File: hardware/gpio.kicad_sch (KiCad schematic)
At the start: 19 parts, among them J3 HDMI_C_1.3, U5 PCA9306DC1

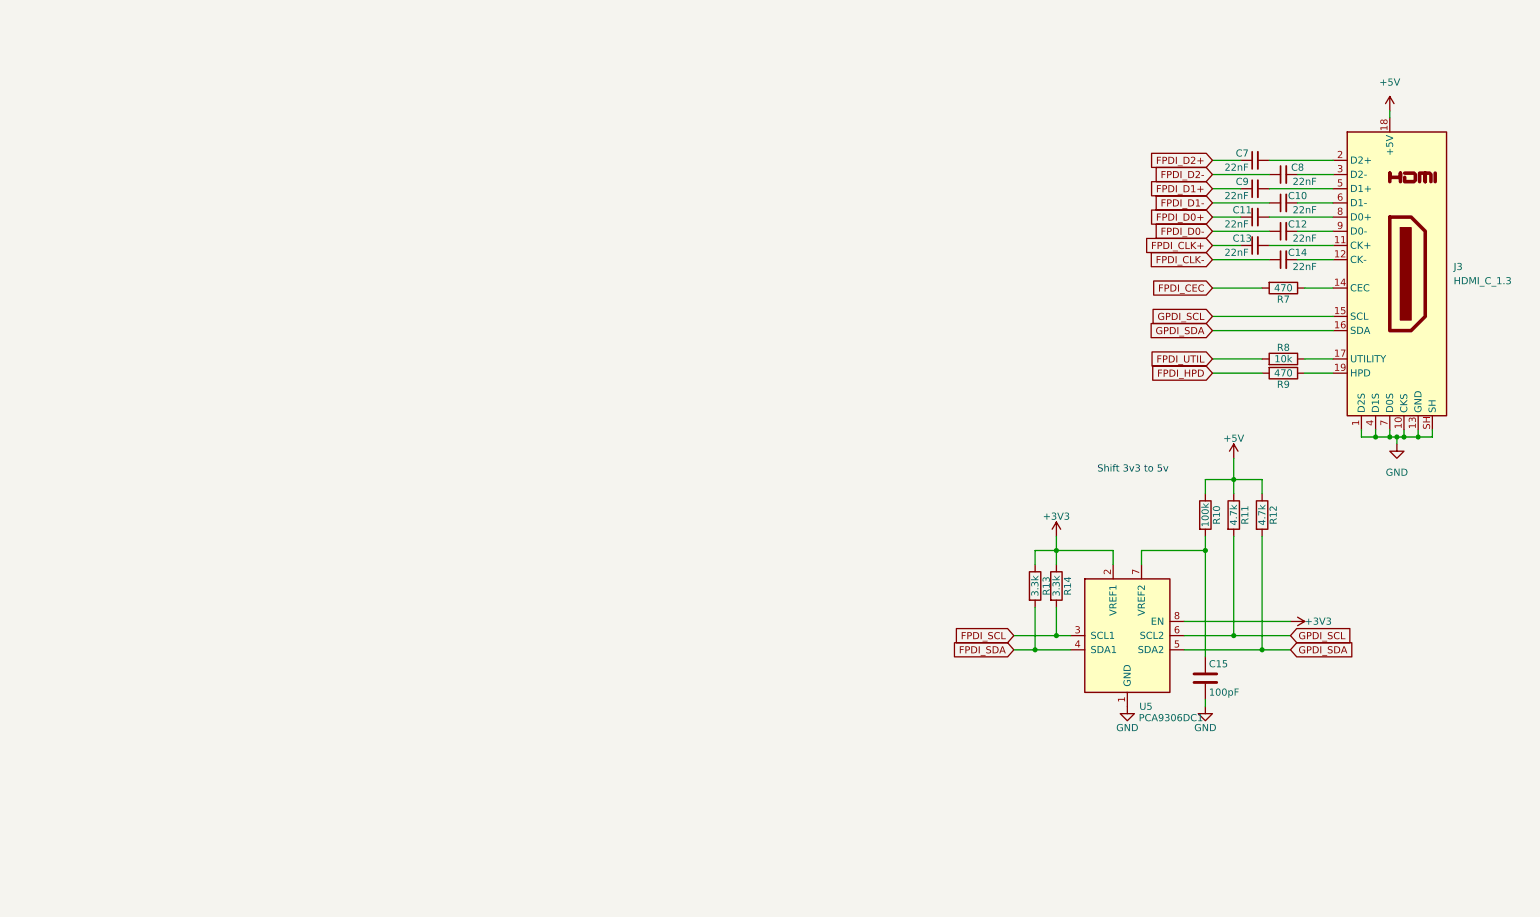
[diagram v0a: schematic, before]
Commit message: Routed most of sdram
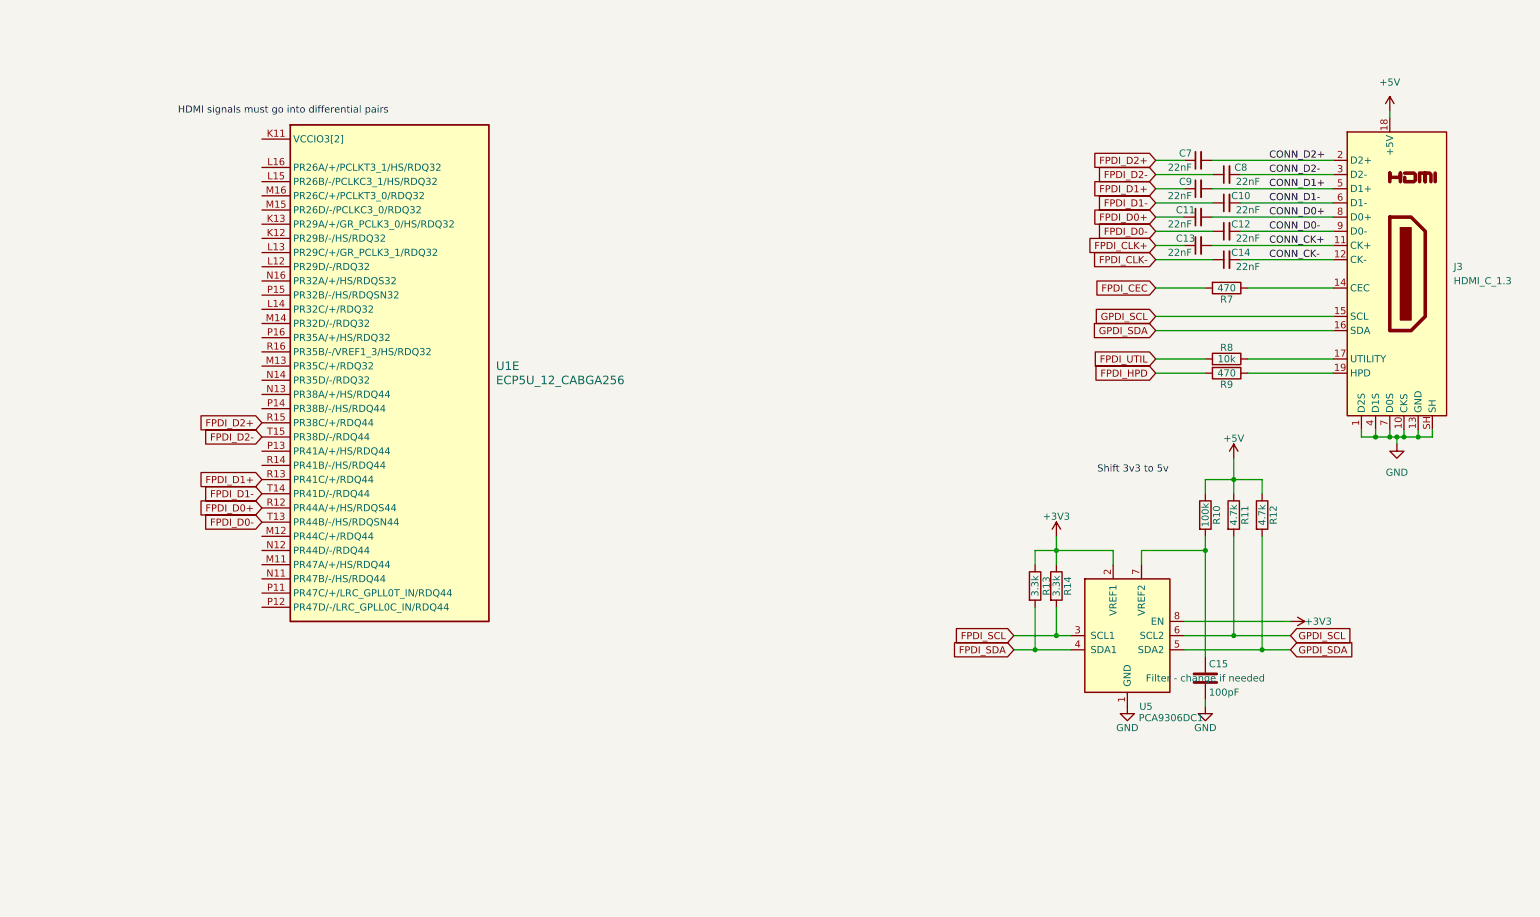
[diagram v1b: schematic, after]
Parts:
- added U1: ECP5U_12_CABGA256, Package_BGA:BGA-256_14.0x14.0mm_Layout16x16_P0.8mm_Ball0.45mm_Pad0.32mm_NSMD, symbol josh:ECP5U_12_CABGA256
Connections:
- net FPDI_D0+: now also U1.R12 (PR44A/+/HS/RDQS44)
- net FPDI_D0-: now also U1.T13 (PR44B/-/HS/RDQSN44)
- net FPDI_D1+: now also U1.R13 (PR41C/+/RDQ44)
- net FPDI_D1-: now also U1.T14 (PR41D/-/RDQ44)
- net FPDI_D2+: now also U1.R15 (PR38C/+/RDQ44)
- net FPDI_D2-: now also U1.T15 (PR38D/-/RDQ44)
- net CONN_D0+: now reaches C11.2, J3.8 (D0+)
- net CONN_D1+: now reaches C9.2, J3.5 (D1+)
- net CONN_D0-: now reaches C12.2, J3.9 (D0-)
- net CONN_CK-: now reaches C14.2, J3.12 (CK-)
- net CONN_D1-: now reaches C10.2, J3.6 (D1-)
- net CONN_D2+: now reaches C7.2, J3.2 (D2+)
- net CONN_CK+: now reaches C13.2, J3.11 (CK+)
- net CONN_D2-: now reaches C8.2, J3.3 (D2-)
- new net: U1.K11 (VCCIO3[2]), U1.L11 (VCCIO3[2])
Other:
- note added: "HDMI signals must go into differential pairs"
- moved on the sheet: C10, C11, C12, C13, C14, C7, C8, C9, R7, R8, R9

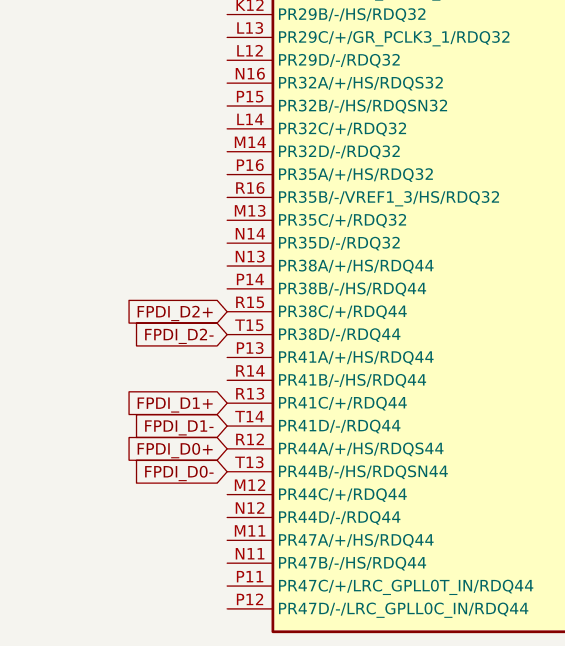
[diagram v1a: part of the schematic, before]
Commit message: Routed power
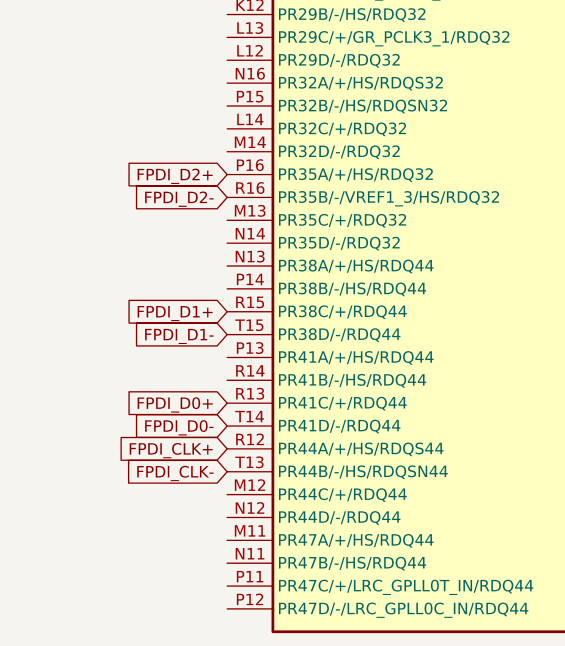
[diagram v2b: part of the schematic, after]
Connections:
- net FPDI_CLK+: now also U1.R12 (PR44A/+/HS/RDQS44)
- net FPDI_CLK-: now also U1.T13 (PR44B/-/HS/RDQSN44)
- net FPDI_D0+: now also U1.R13 (PR41C/+/RDQ44); no longer U1.R12 (PR44A/+/HS/RDQS44)
- net FPDI_D0-: now also U1.T14 (PR41D/-/RDQ44); no longer U1.T13 (PR44B/-/HS/RDQSN44)
- net FPDI_D1+: now also U1.R15 (PR38C/+/RDQ44); no longer U1.R13 (PR41C/+/RDQ44)
- net FPDI_D1-: now also U1.T15 (PR38D/-/RDQ44); no longer U1.T14 (PR41D/-/RDQ44)
- net FPDI_D2+: now also U1.P16 (PR35A/+/HS/RDQ32); no longer U1.R15 (PR38C/+/RDQ44)
- net FPDI_D2-: now also U1.R16 (PR35B/-/VREF1_3/HS/RDQ32); no longer U1.T15 (PR38D/-/RDQ44)

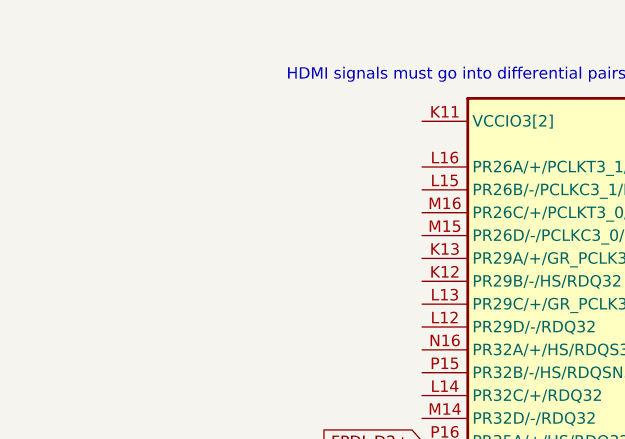
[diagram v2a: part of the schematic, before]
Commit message: Added the decoupling capacitors
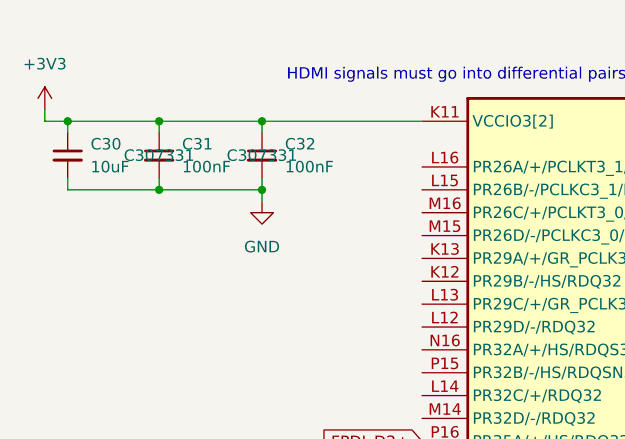
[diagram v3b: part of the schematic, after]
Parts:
- added C30: 10uF, Capacitor_SMD:C_0603_1608Metric, symbol Device:C_Small
- added C31, C32: 100nF, Capacitor_SMD:C_0402_1005Metric, symbol Device:C_Small
- C10, C11, C12, C13, C14, C7, C8, C9: JLCPCB Part # (none) -> C1532
- C15: JLCPCB Part # (none) -> C1546
- J3: footprint cyao:XKB Connection A71-05H4-111N1 -> icepi-lib:XKB Connection A71-05H4-111N1
- R10: JLCPCB Part # (none) -> C25741
- R11, R12: JLCPCB Part # (none) -> C25900
- R13, R14: JLCPCB Part # (none) -> C25890
- R7, R9: JLCPCB Part # (none) -> C25117
- R8: JLCPCB Part # (none) -> C25744
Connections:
- net +3V3: now also U1.K11 (VCCIO3[2]), U1.L11 (VCCIO3[2]), C30.1, C31.1, C32.1
- net GND: now also C30.2, C31.2, C32.2

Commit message: V1.0 Final Revision and Readme documentation
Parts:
- removed U1: ECP5U_12_CABGA256, Package_BGA:BGA-256_14.0x14.0mm_Layout16x16_P0.8mm_Ball0.45mm_Pad0.32mm_NSMD, symbol josh:ECP5U_12_CABGA256
- added U3: ECP5U_12_CABGA256, Package_BGA:BGA-256_14.0x14.0mm_Layout16x16_P0.8mm_Ball0.45mm_Pad0.32mm_NSMD, symbol josh:ECP5U_12_CABGA256
- renumbered C7 to C21, C8 to C22, C9 to C23, C10 to C24, C11 to C25, C12 to C26, C13 to C27, C14 to C28, C15 to C29, C30 to C44, C31 to C45, C32 to C46, J3 to J2, R10 to R11, R11 to R12, R12 to R13, R13 to R14, R14 to R15, R7 to R16, R8 to R17, R9 to R18
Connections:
- net +3V3: now also U3.K11 (VCCIO3[2]), U3.L11 (VCCIO3[2])
- net FPDI_CLK+: now also U3.R12 (PR44A/+/HS/RDQS44)
- net FPDI_CLK-: now also U3.T13 (PR44B/-/HS/RDQSN44)
- net FPDI_D0+: now also U3.R13 (PR41C/+/RDQ44)
- net FPDI_D0-: now also U3.T14 (PR41D/-/RDQ44)
- net FPDI_D1+: now also U3.R15 (PR38C/+/RDQ44)
- net FPDI_D1-: now also U3.T15 (PR38D/-/RDQ44)
- net FPDI_D2+: now also U3.P16 (PR35A/+/HS/RDQ32)
- net FPDI_D2-: now also U3.R16 (PR35B/-/VREF1_3/HS/RDQ32)
- net FPDI_HPD: now also U3.L14 (PR32C/+/RDQ32)
- new net SD_CLK: U3.N16 (PR32A/+/HS/RDQS32)
- new net SD_CMD: U3.P15 (PR32B/-/HS/RDQSN32)
- new net SD_DAT0: U3.P14 (PR38B/-/HS/RDQ44)
- new net SD_DAT1: U3.R14 (PR41B/-/HS/RDQ44)
- new net SD_DAT2: U3.M15 (PR26D/-/PCLKC3_0/RDQ32)
- new net SD_DAT3: U3.M14 (PR32D/-/RDQ32)
- new net SD_DET: U3.M16 (PR26C/+/PCLKT3_0/RDQ32)
- new net ~{USB_DTR}: U3.L15 (PR26B/-/PCLKC3_1/HS/RDQ32)
- new net ~{USB_RTS}: U3.L16 (PR26A/+/PCLKT3_1/HS/RDQ32)
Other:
- moved on the sheet: C21, C22, C23, C24, C25, C26, C27, C28, C29, C44, C45, C46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

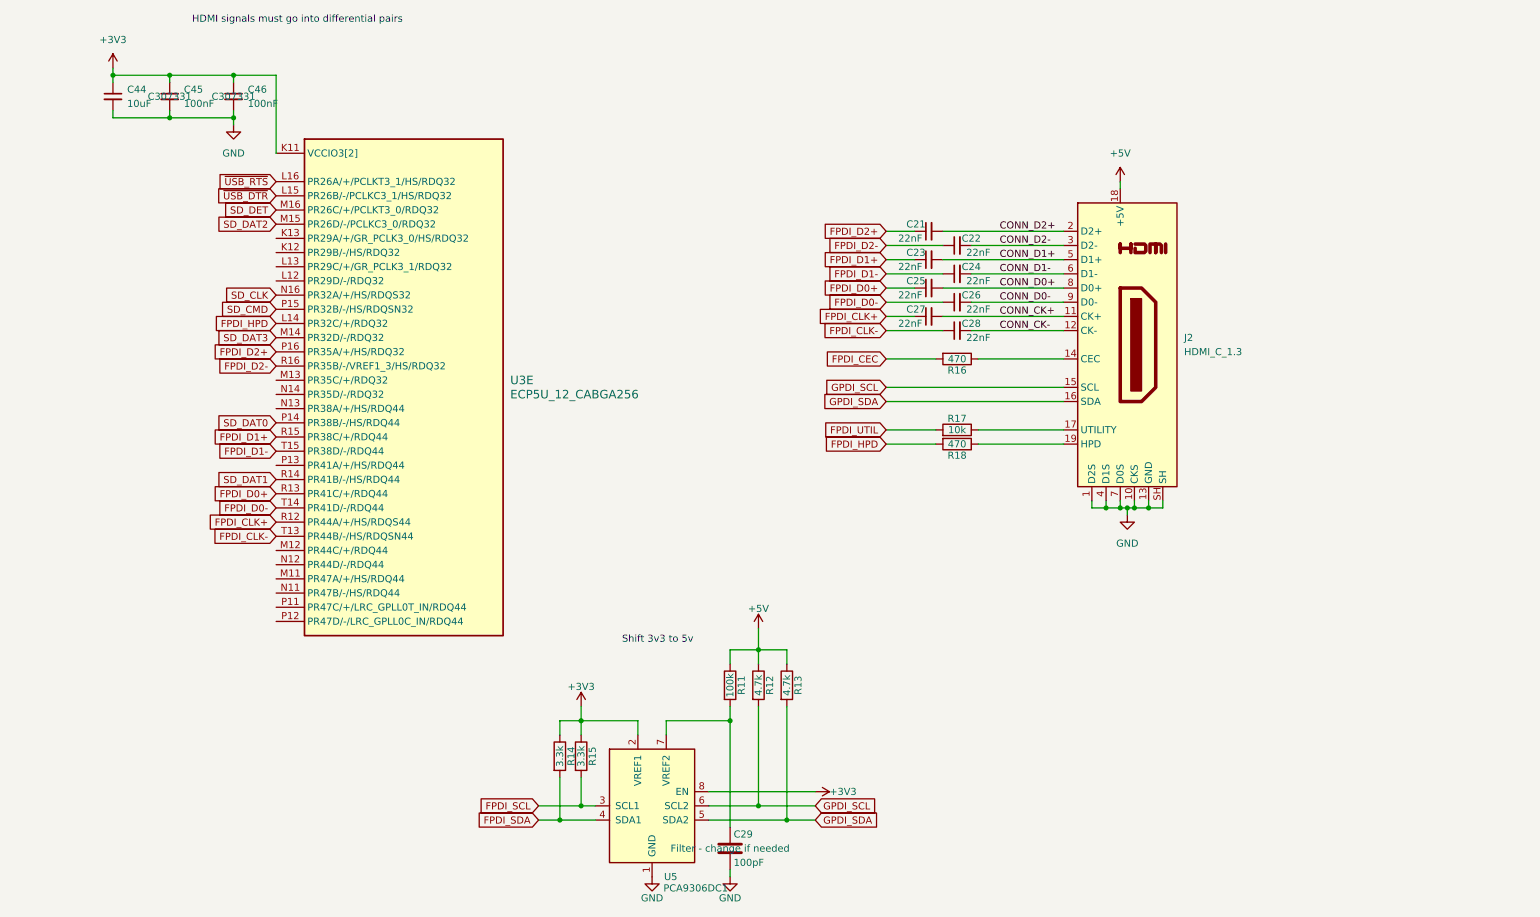
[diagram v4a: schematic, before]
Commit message: Fix level shifter EN voltage error
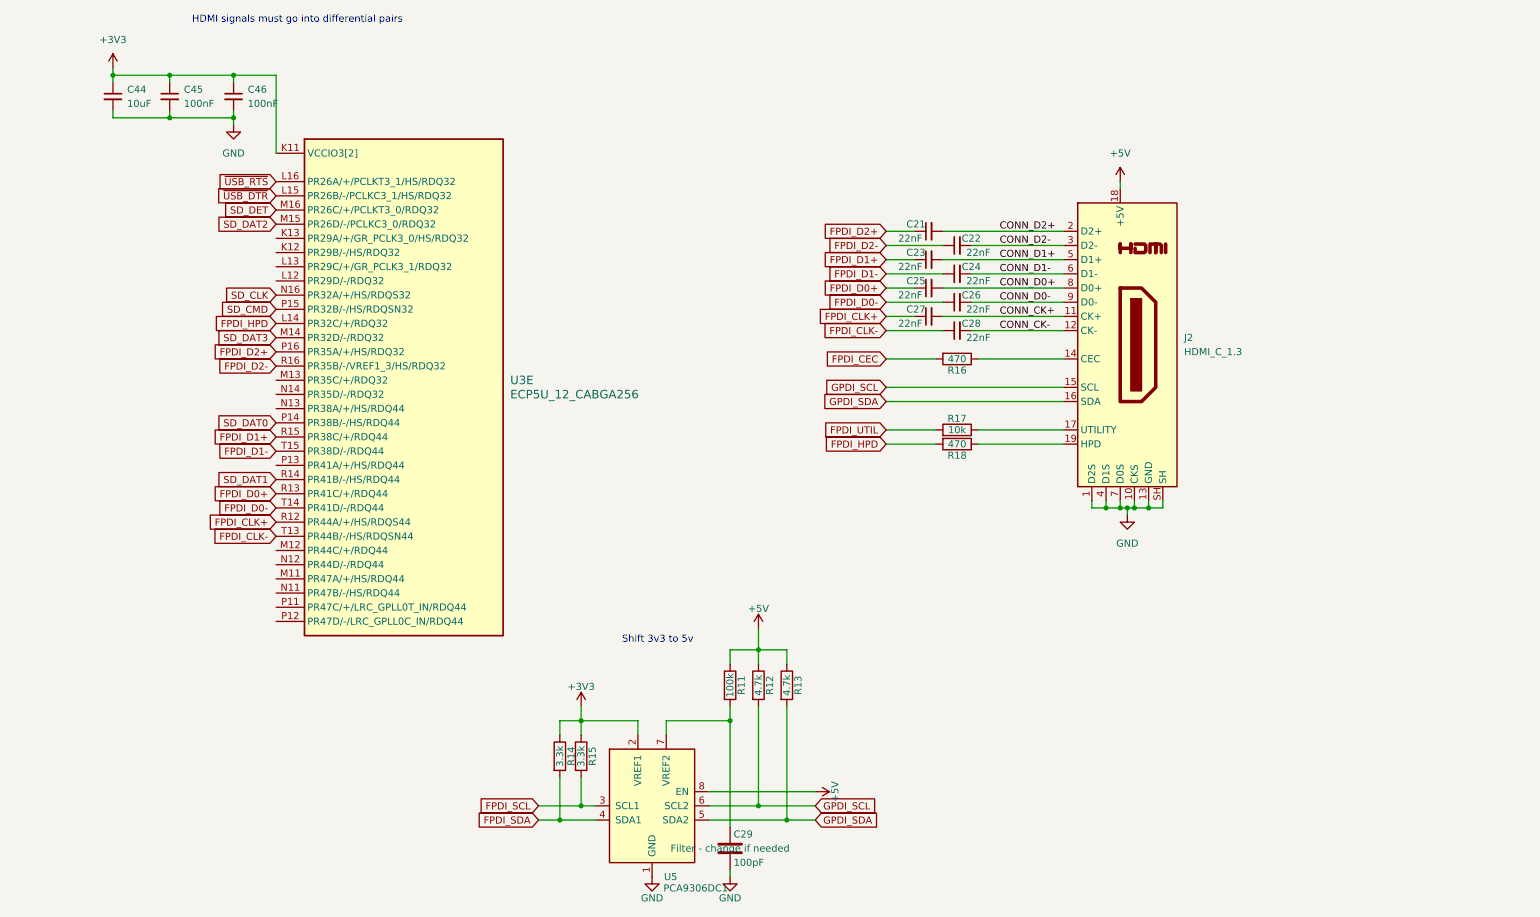
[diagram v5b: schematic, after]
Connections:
- net +3V3: no longer U5.8 (EN)
- net +5V: now also U5.8 (EN)
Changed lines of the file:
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@@
-	)
-	(symbol
-		(lib_id "power:+3V3")
-		(at 158.75 171.45 270)
-		(unit 1)
-		(exclude_from_sim no)
-		(in_bom yes)
-		(on_board yes)
-		(dnp no)
-		(property "Reference" "#PWR039"
-			(at 154.94 171.45 0)
-			(effects
-				(font
-					(size 1.27 1.27)
-				)
-				(hide yes)
-			)
-		)
-		(property "Value" "+3V3"
-			(at 161.29 171.45 90)
-			(effects
-				(font
-					(size 1.27 1.27)
-				)
-				(justify left)
-			)
-		)
-		(property "Footprint" ""
-			(at 158.75 171.45 0)
-			(effects
-				(font
-					(size 1.27 1.27)
-				)
-				(hide yes)
-			)
-		)
-		(property "Datasheet" ""
-			(at 158.75 171.45 0)
-			(effects
-				(font
-					(size 1.27 1.27)
-				)
-				(hide yes)
-			)
-		)
-		(property "Description" ""
-			(at 158.75 171.45 0)
-			(effects
-				(font
-					(size 1.27 1.27)
-				)
-			)
-		)
-		(pin "1"
-		)
-		(instances
-			(project "icepi-zero"
-				(path "/f88da08e-cf42-4d03-a08f-3f602fe6658d/efe0a411-ae63-4682-aa63-a9a30697cd67"
-					(reference "#PWR039")
-					(unit 1)
-				)
-			)
-		)
 	)
 	(symbol
@@
 					(size 1.27 1.27)
 				)
+				(hide yes)
 			)
 		)
@@
 					(size 1.27 1.27)
 				)
+				(hide yes)
 			)
 		)
@@
 					(unit 1)
 				)
+			)
+		)
+	)
+	(symbol
+		(lib_id "power:+5V")
+		(at 158.75 171.45 270)
+		(unit 1)
+		(exclude_from_sim no)
+		(in_bom yes)
+		(on_board yes)
+		(dnp no)
+		(property "Reference" "#PWR039"
+			(at 154.94 171.45 0)
+			(effects
+				(font
+					(size 1.27 1.27)
+				)
+				(hide yes)
+			)
+		)
+		(property "Value" "+5V"
+			(at 162.306 171.45 0)
+			(effects
+				(font
+					(size 1.27 1.27)
+				)
+			)
+		)
+		(property "Footprint" ""
+			(at 158.75 171.45 0)
+			(effects
+				(font
+					(size 1.27 1.27)
+				)
+			)
+		)
+		(property "Datasheet" ""
+			(at 158.75 171.45 0)
+			(effects
+				(font
+					(size 1.27 1.27)
+				)
+			)
+		)
+		(property "Description" ""
+			(at 158.75 171.45 0)
+			(effects
+				(font
+					(size 1.27 1.27)
+				)
+			)
+		)
+		(pin "1"
+		)
+		(instances
+			(project "icepi-zero"
+				(path "/f88da08e-cf42-4d03-a08f-3f602fe6658d/efe0a411-ae63-4682-aa63-a9a30697cd67"
+					(reference "#PWR039")
+					(unit 1)
+				)

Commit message: Add a revision
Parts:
- R16, R18: JLCPCB Part # C25117 -> C25117
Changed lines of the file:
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@@
 			)
 		)
-		(property "JLCPCB Part #" "C25117 "
+		(property "JLCPCB Part #" "C25117"
 			(at 184.15 109.22 0)
 			(effects
@@
 			)
 		)
-		(property "JLCPCB Part #" "C25117 "
+		(property "JLCPCB Part #" "C25117"
 			(at 184.15 93.98 0)
 			(effects

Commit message: Pre-prod fixes
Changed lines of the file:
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@@
 					(size 1.27 1.27)
 				)
+				(hide yes)
 			)
 		)
@@
 		(on_board yes)
 		(dnp no)
-		(fields_autoplaced yes)
 		(property "Reference" "U3"
 			(at 104.14 97.7899 0)
